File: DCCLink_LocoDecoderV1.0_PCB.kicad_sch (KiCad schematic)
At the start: 18 parts, among them J1 USB_B_Micro, Q1 BC847BS, U1 ESP32-WROOM-32U, U2 AMS1117-3.3, U3 AMS1117-5.0, U4 CH340C, U5 USBLC6-2SC6, U6 DRV8871DDA

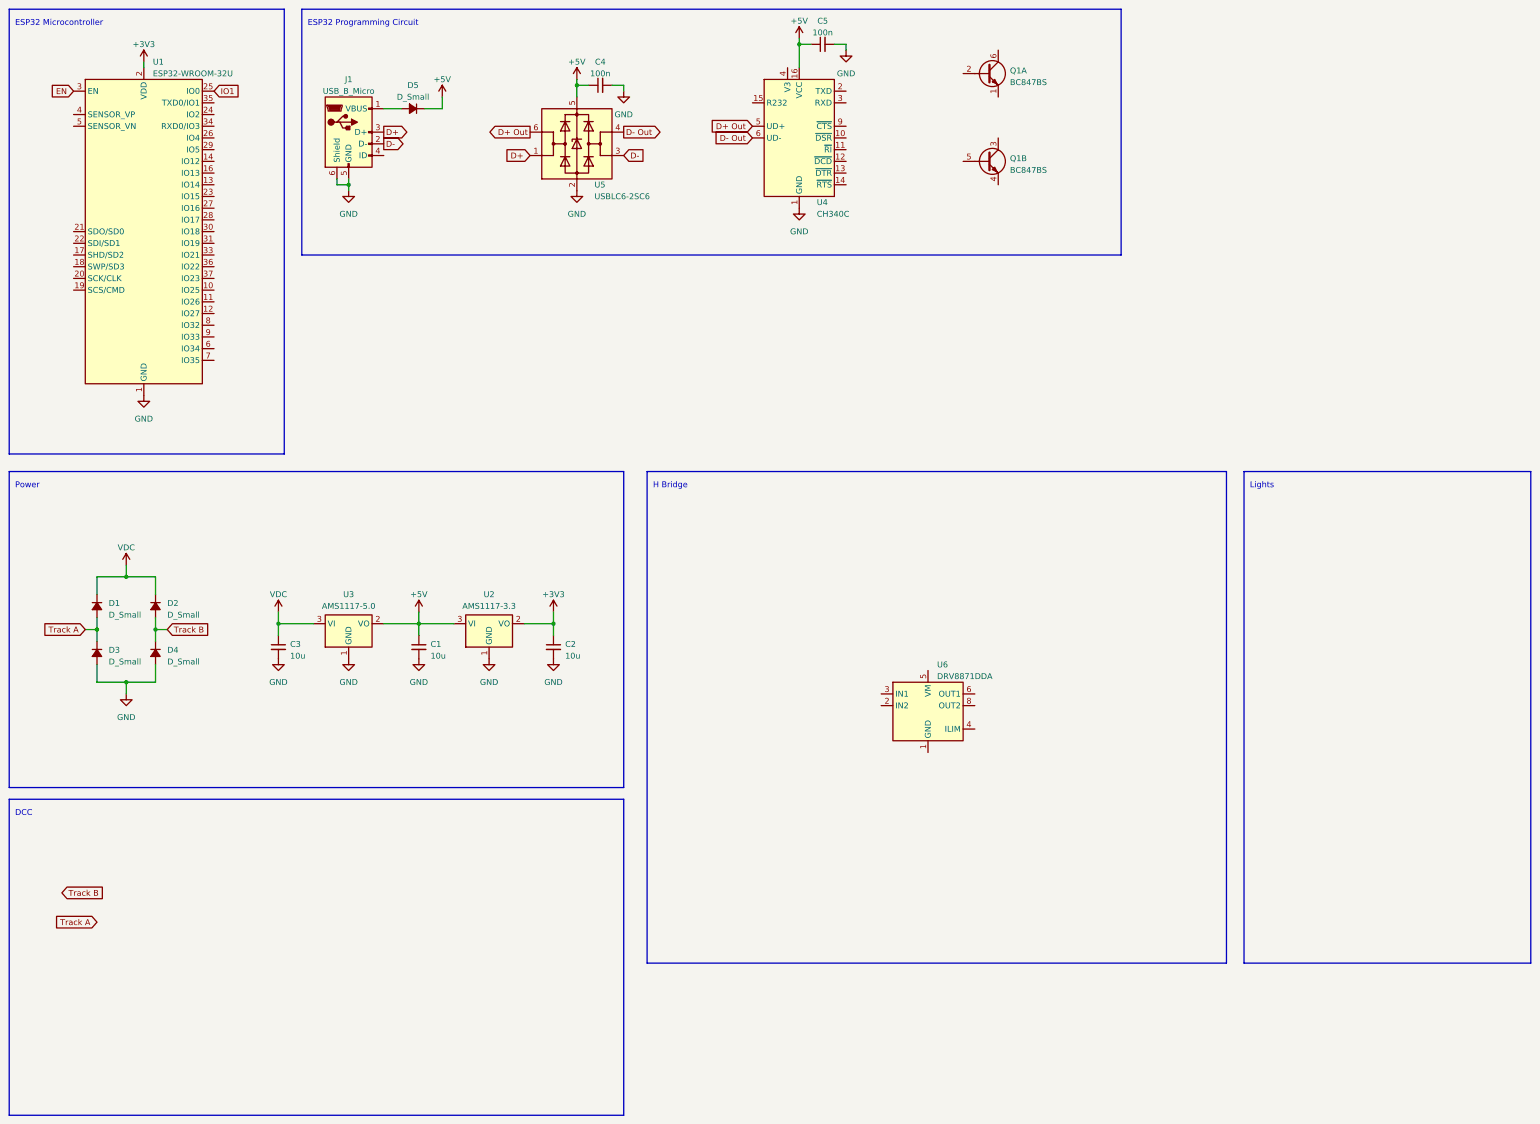
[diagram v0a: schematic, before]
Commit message: Chose Optocoupler and Motor Driver
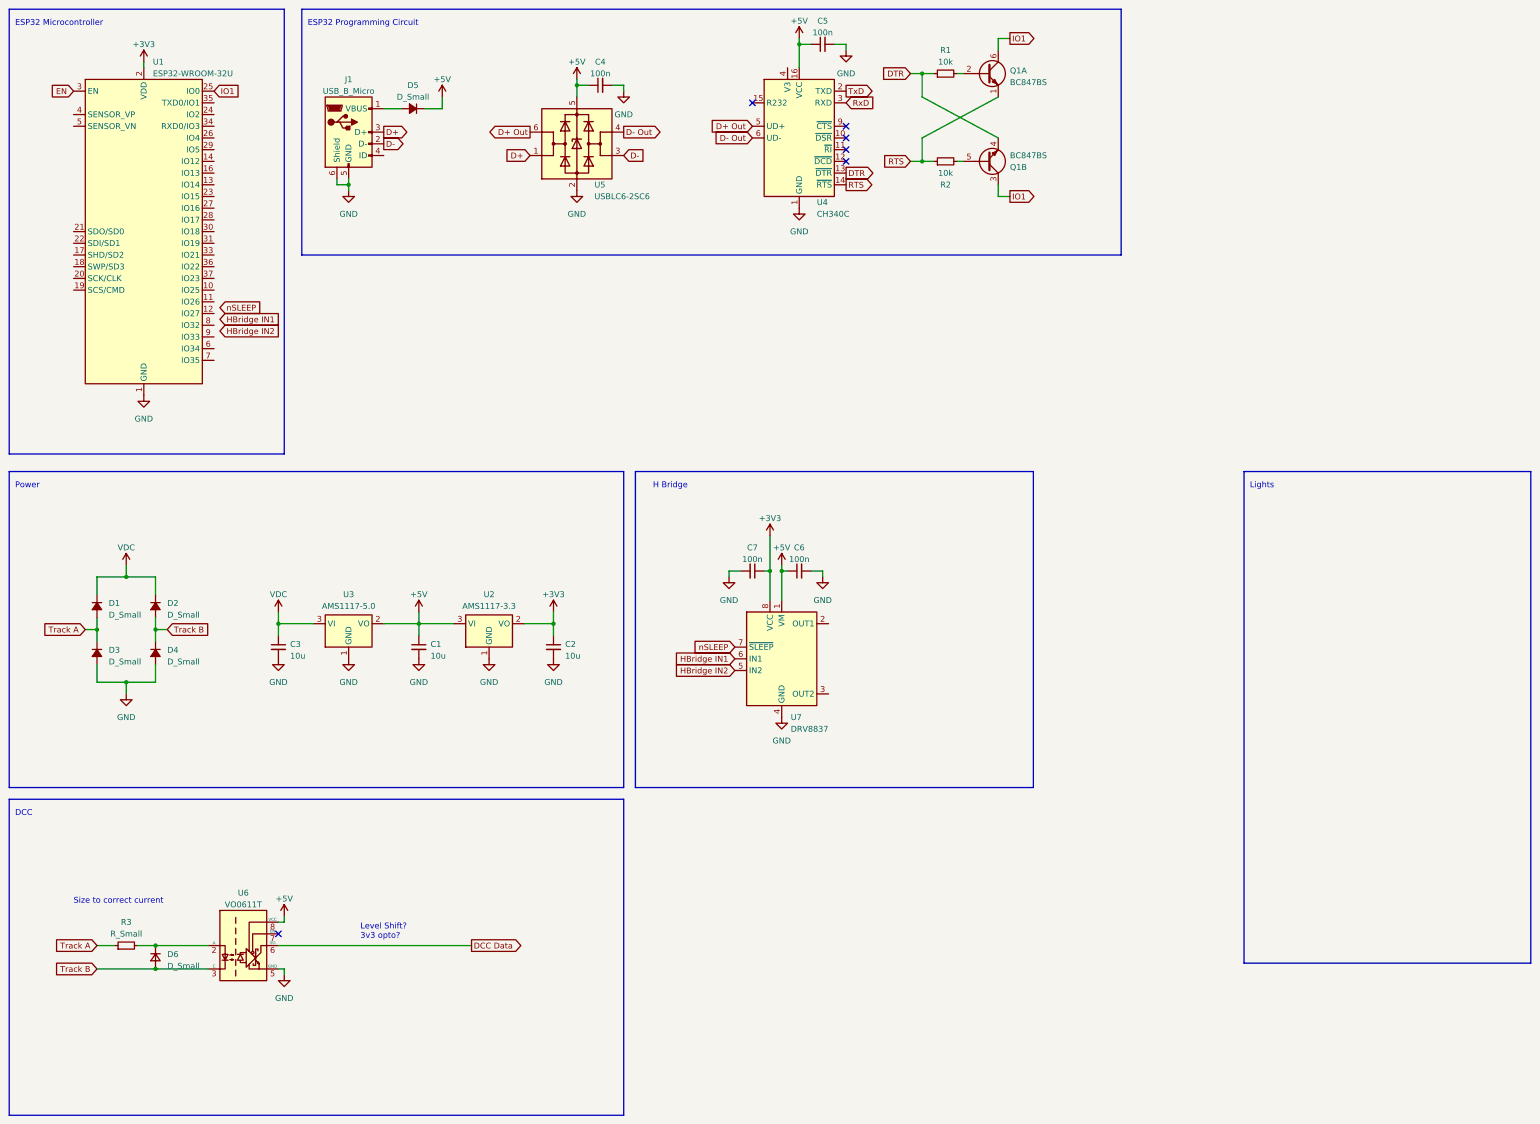
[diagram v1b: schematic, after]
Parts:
- removed U6: DRV8871DDA, Package_SO:Texas_HTSOP-8-1EP_3.9x4.9mm_P1.27mm_EP2.95x4.9mm_Mask2.4x3.1mm_ThermalVias, symbol Driver_Motor:DRV8871DDA
- added C6, C7: 100n, symbol Device:C_Small
- added D6: D_Small, symbol Device:D_Small
- added R1, R2: 10k, symbol Device:R_Small
- added R3: R_Small, symbol Device:R_Small
- added U6: VO0611T, Package_SO:SOIC-8_3.9x4.9mm_P1.27mm, symbol Isolator:VO0611T
- added U7: DRV8837, Package_SON:WSON-8-1EP_2x2mm_P0.5mm_EP0.9x1.6mm, symbol Driver_Motor:DRV8837
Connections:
- net +3V3: now also C7.1, U7.8 (VCC)
- net +5V: now also C6.1, U6.8 (VCC), U7.1 (VM)
- net GND: now also C6.2, C7.2, U6.5 (GND), U7.4 (GND), U7.9 (GND)
- net IO1: now also Q1.3 (C2), Q1.6 (C1)
- net Track A: now also R3.1
- net Track B: now also D6.2 (A), U6.3 (C)
- net DTR: now reaches Q1.4 (E2)
- net DTR: now also U4.13 (~{DTR}), R1.1
- net at Q1.5 (B2): now also R2.2
- net RTS: now reaches Q1.1 (E1)
- net RTS: now also U4.14 (~{RTS}), R2.1
- net at Q1.2 (B1): now also R1.2
- net TxD: now reaches U4.2 (TXD)
- net RxD: now reaches U4.3 (RXD)
- new net: D6.1 (K), R3.2, U6.2 (A)
- new net DCC Data: U6.6 (VO)
- new net HBridge IN1: U7.6 (IN1)
- new net HBridge IN2: U7.5 (IN2)
- new net nSLEEP: U7.7 (~{SLEEP})
- no-connect marks 0 -> 6
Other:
- note added: "Level Shift? 3v3 opto?"
- note added: "Size to correct current"

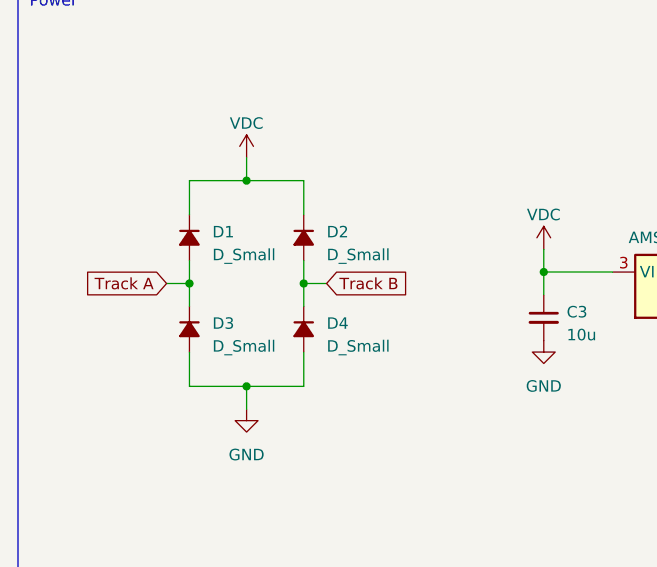
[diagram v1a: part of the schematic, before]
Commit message: Chose Rectifier Diodes
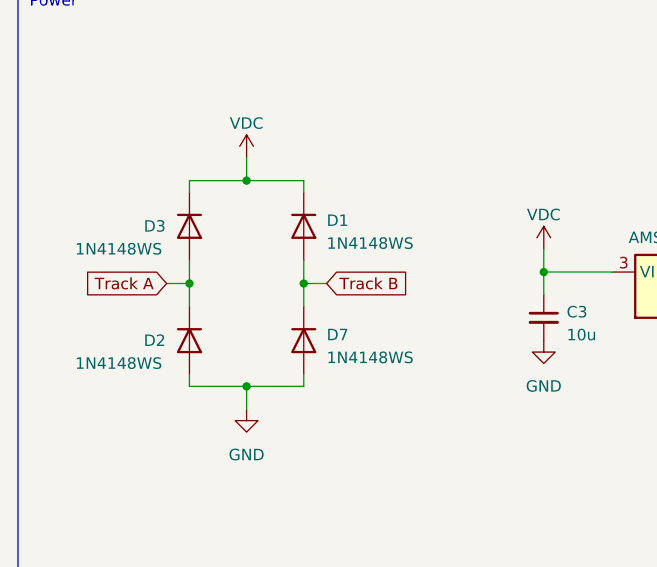
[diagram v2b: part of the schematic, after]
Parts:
- removed D1, D2, D3, D4: D_Small, symbol Device:D_Small_Filled
- added D1, D2, D3, D7: 1N4148WS, Diode_SMD:D_SOD-323, symbol Diode:1N4148WS
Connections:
- net GND: now also D2.2 (A), D7.2 (A)
- net Track A: now also D2.1 (K), D3.2 (A)
- net Track B: now also D1.2 (A), D7.1 (K)
- net VDC: now also D1.1 (K), D3.1 (K)
